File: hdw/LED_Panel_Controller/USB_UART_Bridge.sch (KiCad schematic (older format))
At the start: 42 parts

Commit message: made a lot more schematic progress
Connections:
- net USB_UART_RX is gone; now on net PIC32MZ_UART_RX: R?.2, U?.2 (A1)
- net USB_UART_TX is gone; now on net PIC32MZ_UART_TX: R?.2, U?.3 (A2)
- net +3.3V_USB: no longer R?.1, R?.1, R?.1, R?.1
- net +3V3: now also R?.1, R?.1, R?.1, R?.1
- net WIFI_UART_RX: now also R?.1, U?.23 (S:GPIO.1/DTR)
- net WIFI_UART_TX: now also R?.1, U?.24 (S:GPIO.0/DCD)
- net PIC32MZ_UART_RX: now reaches R?.1, U?.14 (E:GPIO.1/DSR)
- net PIC32MZ_UART_TX: now reaches R?.1, U?.15 (E:GPIO.0/DTR)
- net USB_UART_RX_BUF renamed PIC32MZ_UART_RX_BUF
- net USB_UART_TX_BUF renamed PIC32MZ_UART_TX_BUF
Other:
- moved on the sheet: D?, R?

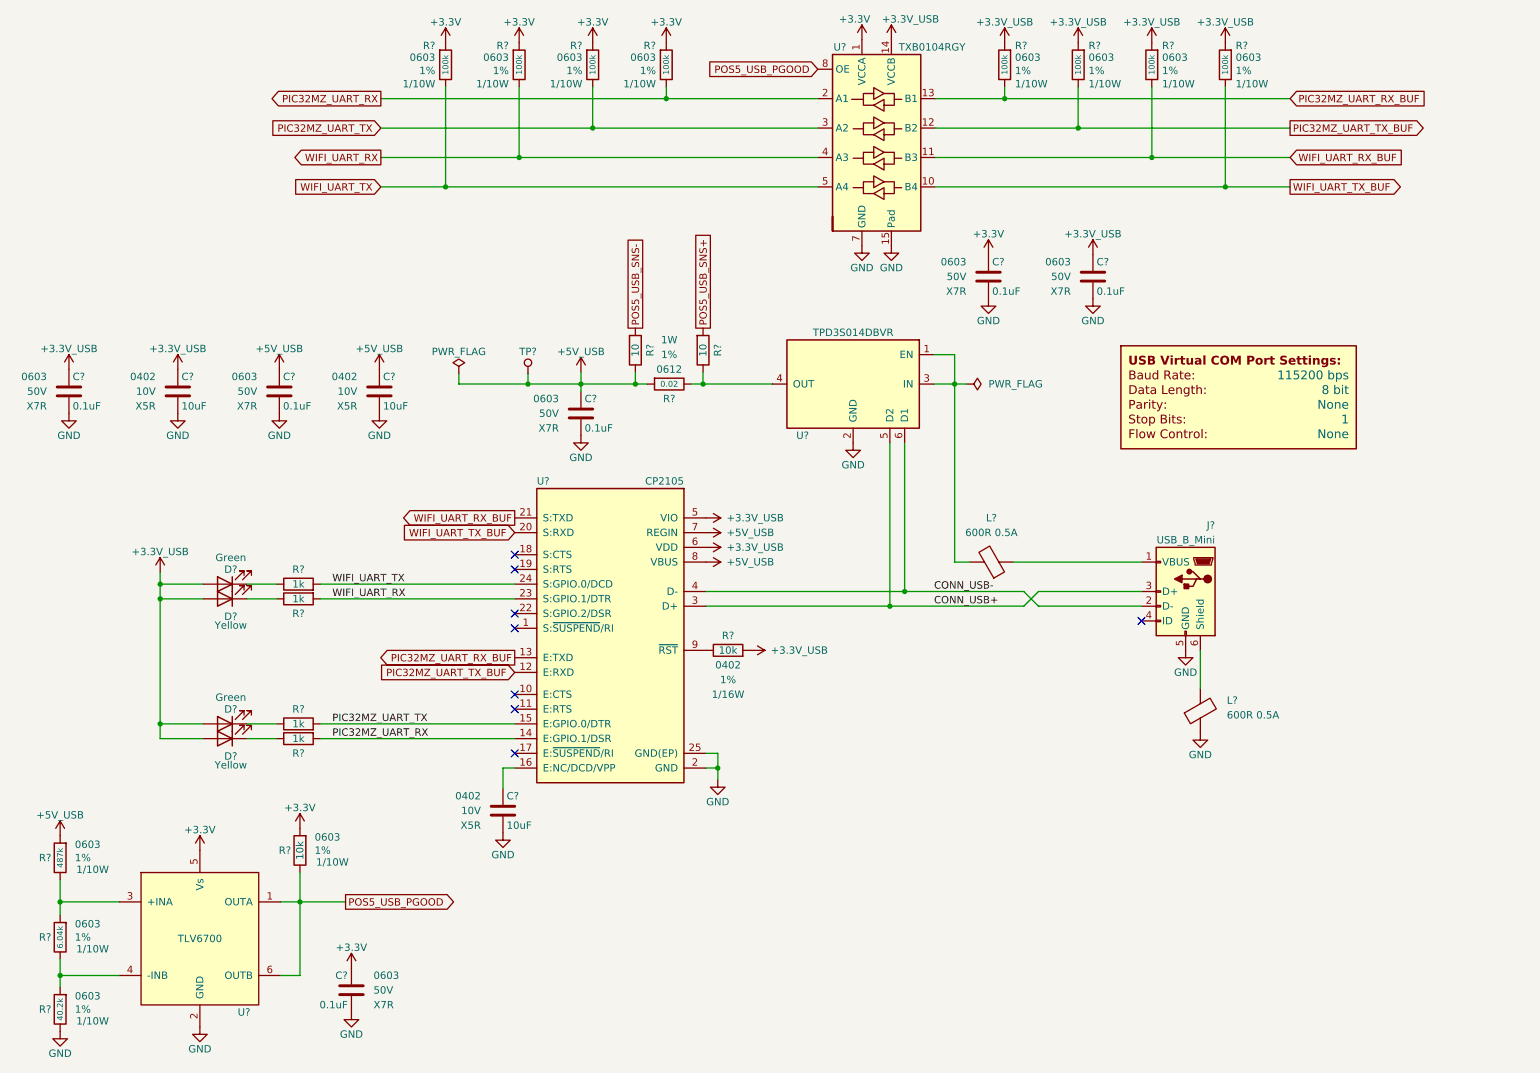
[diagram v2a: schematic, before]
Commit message: lots of MCU pin assignments
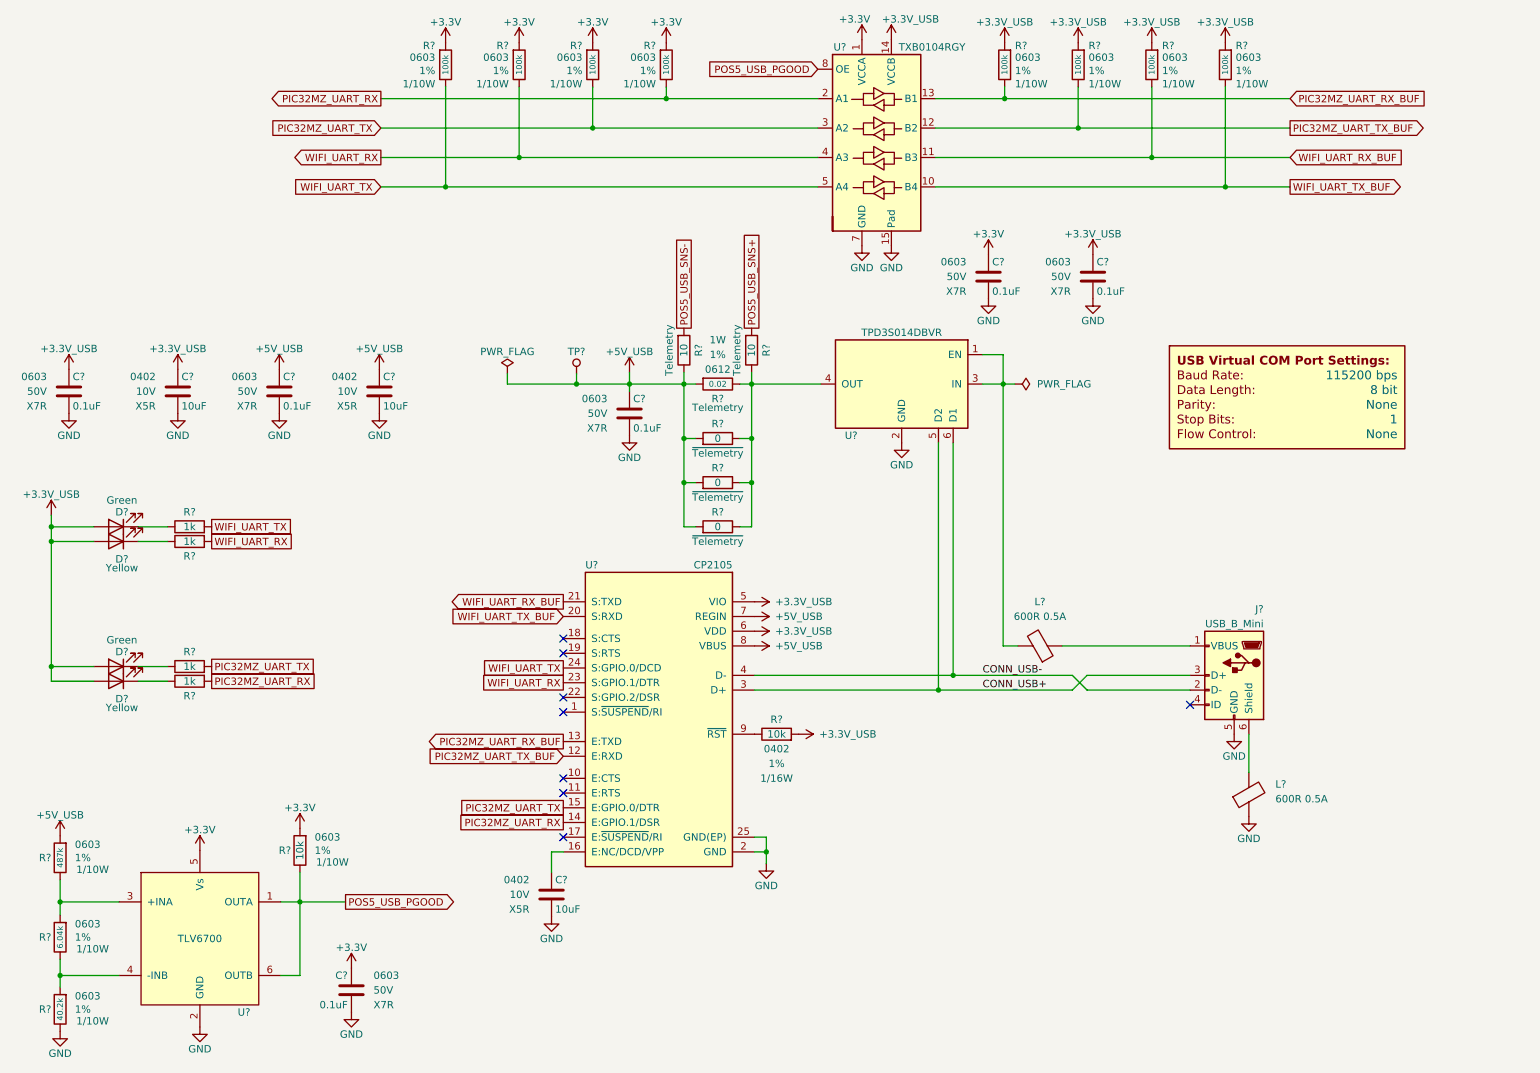
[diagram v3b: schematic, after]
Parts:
- removed R?: 10, Resistors_SMD:R_0603, symbol Custom_Library:R_Custom
- added R? (x3): 0, Resistors_SMD:R_0402, symbol Custom_Library:R_Custom
- added R?: 10, Resistors_SMD:R_0603, symbol Custom_Library:R_Custom
- R? (x2): Configuration (none) -> Telemetry
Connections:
- net +5V_USB: now also R?.1, R?.1, R?.1
- net POS5_USB_SNS+: now also R?.1
- net at R?.2, U?.4 (OUT): now also R?.2, R?.2, R?.2, R?.2
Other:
- moved on the sheet: C?, D?, J?, L?, R?, TP?, U?

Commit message: more schematic progress
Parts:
- added DOC?: COM_Port_Settings, symbol Custom_Library:COM_Port_Settings
- DOC?: Baud_Rate 115200 bps -> 921600 bps
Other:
- note added: "Enumerates as two COM port endpoints:\nFirst for PIC32MZ, second for ATWINC1500 WiFi module"
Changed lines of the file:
@@
 F 2 "" H 9210 3880 60  0001 C CNN
 F 3 "" H 9210 3880 60  0001 C CNN
-F 4 "115200 bps" H 9960 3530 60  0000 R CNN "Baud_Rate"
+F 4 "921600 bps" H 9960 3530 60  0000 R CNN "Baud_Rate"
 F 5 "8 bit" H 9960 3430 60  0000 R CNN "Data_Length"
 F 6 "None" H 9960 3330 60  0000 R CNN "Parity"
@@
 	-1   0    0    -1
 $EndComp
+$Comp
+L Custom_Library:COM_Port_Settings DOC?
+U 1 1 601B933A
+P 9210 4190
+F 0 "DOC?" H 9210 4590 60  0001 C CNN
+F 1 "COM_Port_Settings" H 9210 4690 60  0001 C CNN
+F 2 "" H 9210 4690 60  0001 C CNN
+F 3 "" H 9210 4690 60  0001 C CNN
+F 4 "115200 bps" H 9960 4340 60  0000 R CNN "Baud_Rate"
+F 5 "8 bit" H 9960 4240 60  0000 R CNN "Data_Length"
+F 6 "None" H 9960 4140 60  0000 R CNN "Parity"
+F 7 "1" H 9960 4040 60  0000 R CNN "Stop_Bits"
+F 8 "None" H 9960 3940 60  0000 R CNN "Flow_Control"
+	1    9210 4190
+	1    0    0    -1
+$EndComp
+Text Notes 8280 2890 0    50   ~ 0
+Enumerates as two COM port endpoints:\nFirst for PIC32MZ, second for ATWINC1500 WiFi module
 $EndSCHEMATC

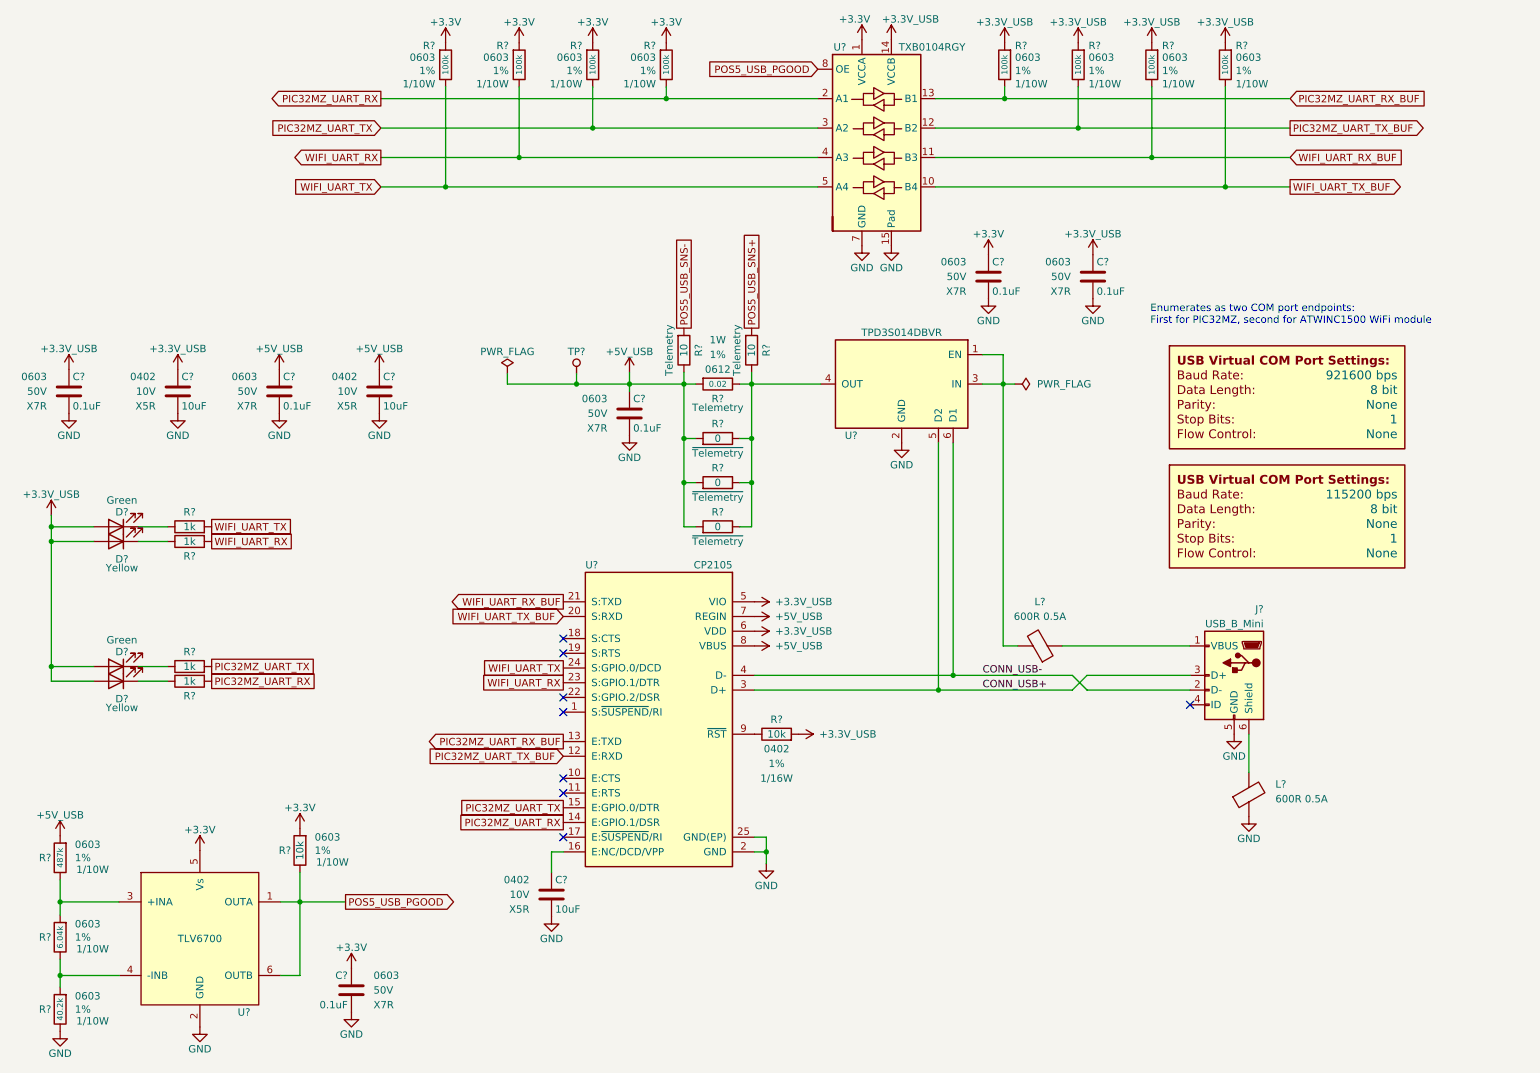
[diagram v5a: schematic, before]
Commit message: added digikey pns, footprints, bom scrubbed
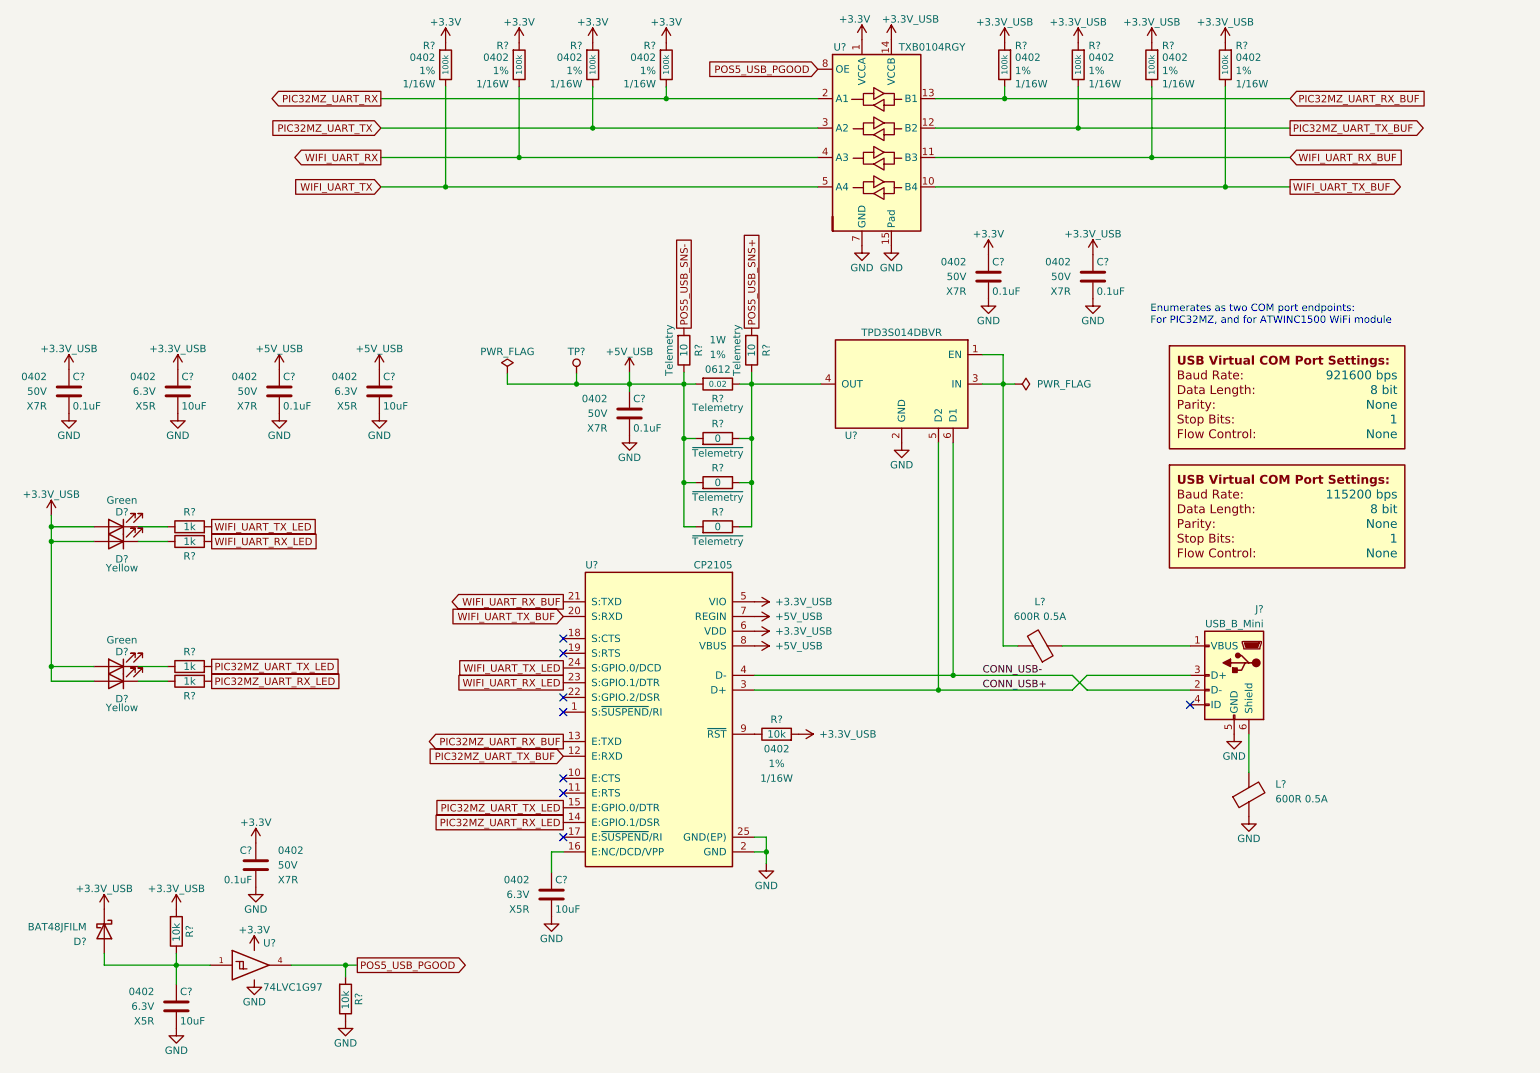
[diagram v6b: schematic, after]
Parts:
- removed C?: 0.1uF, Capacitors_SMD:C_0603, symbol Custom_Library:C_Custom
- removed R?: 6.04k, Resistors_SMD:R_0603, symbol Custom_Library:R_Custom
- removed R?: 40.2k, Resistors_SMD:R_0603, symbol Custom_Library:R_Custom
- removed R?: 487k, Resistors_SMD:R_0603, symbol Custom_Library:R_Custom
- removed R?: 10k, Resistors_SMD:R_0603, symbol Custom_Library:R_Custom
- removed U?: TLV6700, Package_TO_SOT_SMD:SOT-23-6, symbol Custom_Library:TLV6700
- added C?: 0.1uF, Capacitors_SMD:C_0402, symbol Custom_Library:C_Custom
- added C?: 10uF, Capacitors_SMD:C_0402, symbol Custom_Library:C_Custom
- added D?: BAT48JFILM, Diode_SMD:D_SOD-323, symbol Diode:BAT48JFILM
- added R? (x2): 10k, Resistors_SMD:R_0402, symbol Custom_Library:R_Custom
- added U?: 74LVC1G97, Package_TO_SOT_SMD:SOT-363_SC-70-6, symbol Custom_Library:74LVC1G97_Power_BUF
- C? (x5): footprint Capacitors_SMD:C_0603 -> Capacitors_SMD:C_0402; Digi-Key PN 399-7845-1-ND -> 490-10701-1-ND; display_footprint 0603 -> 0402
- C? (x3): footprint (none) -> Capacitors_SMD:C_0402; Digi-Key PN 1276-6830-1-ND -> 1276-1451-1-ND; Voltage 10V -> 6.3V
- D? (x2): footprint LEDs:LED_0603 -> LEDs:LED_0402; Digi-Key PN 754-1121-1-ND -> 1497-1219-1-ND
- D? (x2): footprint (none) -> LEDs:LED_0402; Digi-Key PN (none) -> 1497-1198-1-ND
- L? (x2): footprint Inductors_SMD:L_0603 -> Inductors_SMD:L_0402; Digi-Key PN 732-1593-1-ND -> 490-5441-1-ND
- R? (x2): footprint Resistors_SMD:R_0603 -> Resistors_SMD:R_0402; Digi-Key PN YAG2321CT-ND -> RMCF0402FT10R0CT-ND; Wattage 1/10W -> 1/16W; display_footprint 0603 -> 0402
- R? (x8): footprint Resistors_SMD:R_0603 -> Resistors_SMD:R_0402; Digi-Key PN RMCF0603FT100KCT-ND -> RMCF0402FT100KCT-ND; Wattage 1/10W -> 1/16W; display_footprint 0603 -> 0402
- R? (x4): Digi-Key PN (none) -> RMCF0402FT1K00CT-ND
- R? (x3): Digi-Key PN 2019-RK73Z1ETTPCT-ND -> RMCF0402ZT0R00CT-ND
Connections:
- net +3.3V_USB: now also D?.1 (K), R?.1
- net +3V3: now also C?.1, U?.5 (VCC)
- net GND: now also C?.2, C?.2, R?.2, U?.2 (GND), U?.3 (GND), U?.6 (GND)
- net PIC32MZ_UART_RX: no longer R?.1, U?.14 (E:GPIO.1/DSR)
- net PIC32MZ_UART_TX: no longer R?.1, U?.15 (E:GPIO.0/DTR)
- net POS5_USB_PGOOD: now also R?.1, U?.4
- net WIFI_UART_RX: no longer R?.1, U?.23 (S:GPIO.1/DTR)
- net WIFI_UART_TX: no longer R?.1, U?.24 (S:GPIO.0/DCD)
- new net: C?.1, D?.2 (A), R?.2, U?.1
- new net PIC32MZ_UART_RX_LED: R?.1, U?.14 (E:GPIO.1/DSR)
- new net PIC32MZ_UART_TX_LED: R?.1, U?.15 (E:GPIO.0/DTR)
- new net WIFI_UART_RX_LED: R?.1, U?.23 (S:GPIO.1/DTR)
- new net WIFI_UART_TX_LED: R?.1, U?.24 (S:GPIO.0/DCD)
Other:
- note added: "Enumerates as two COM port endpoints:\nFor PIC32MZ, and for ATWINC1500 WiFi module"
- note removed: "Enumerates as two COM port endpoints:\nFirst for PIC32MZ, second for ATWINC1500 WiFi module"

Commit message: assigned I2C addresses
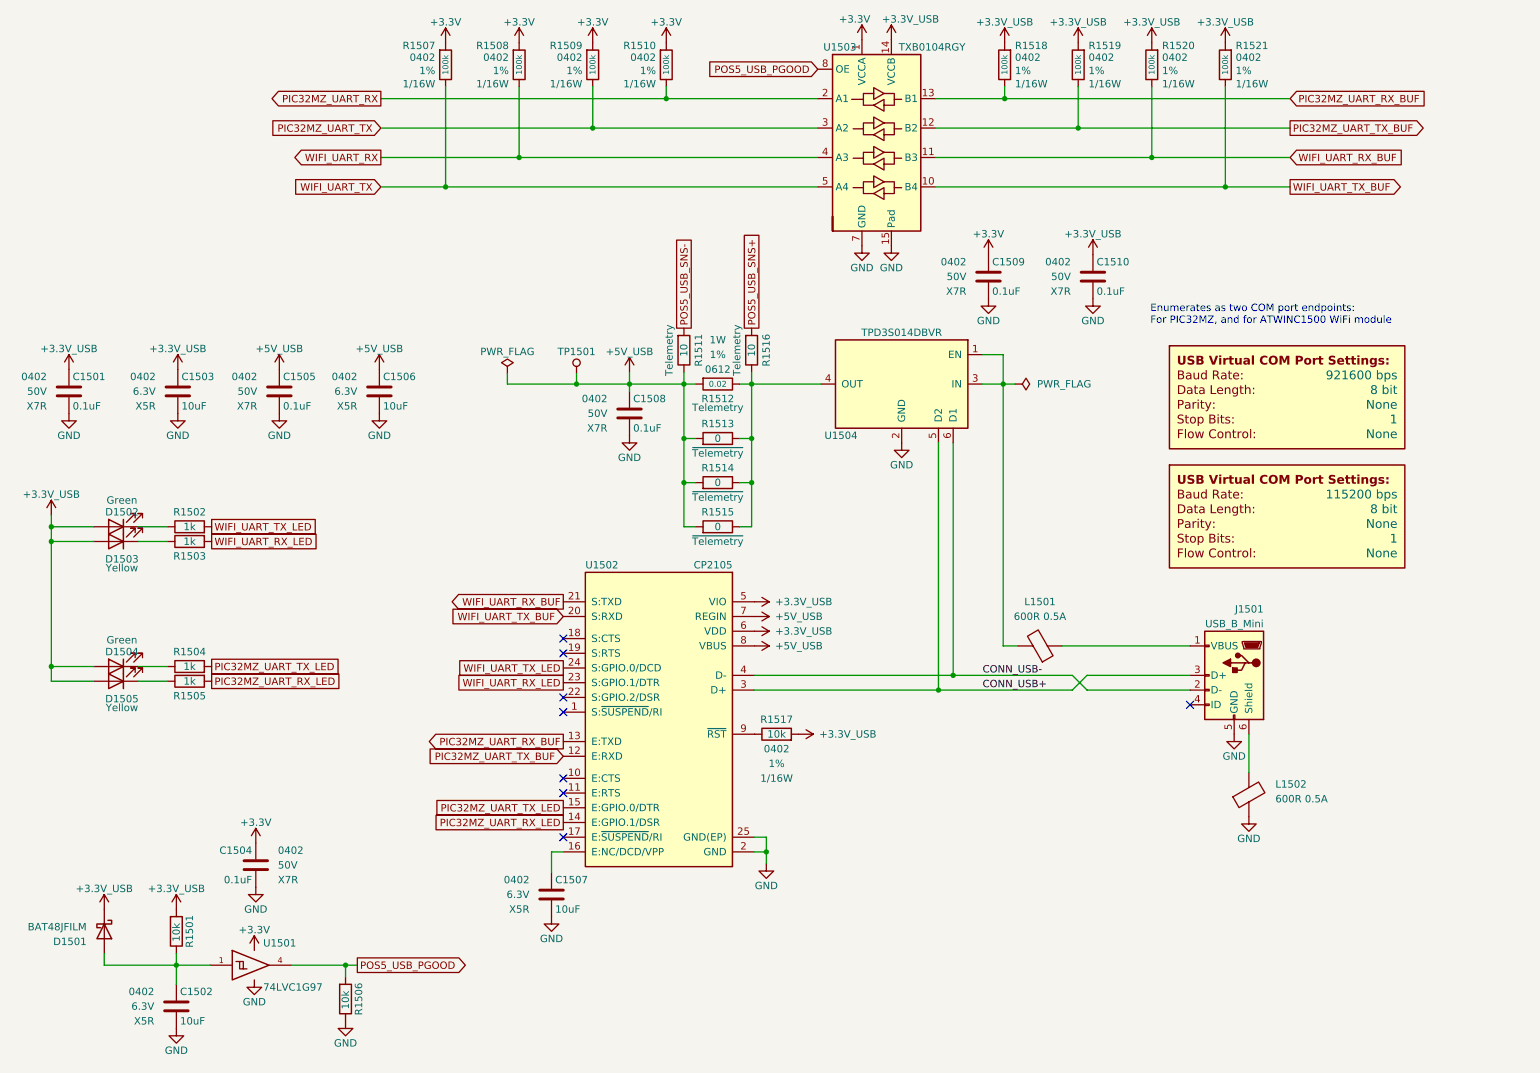
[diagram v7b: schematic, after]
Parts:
- gave numbers to parts that had none: 46
